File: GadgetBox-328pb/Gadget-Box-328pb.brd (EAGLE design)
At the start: 93.5 x 53.5 mm, 35 parts, among them IC1A ATMEGA328PB-AU, IC1B ATMEGA328PB-MU, U1 MCP73831T-2ACI/OT, U2 AP2112-3.3, X1 CRYSTAL-0500290P1

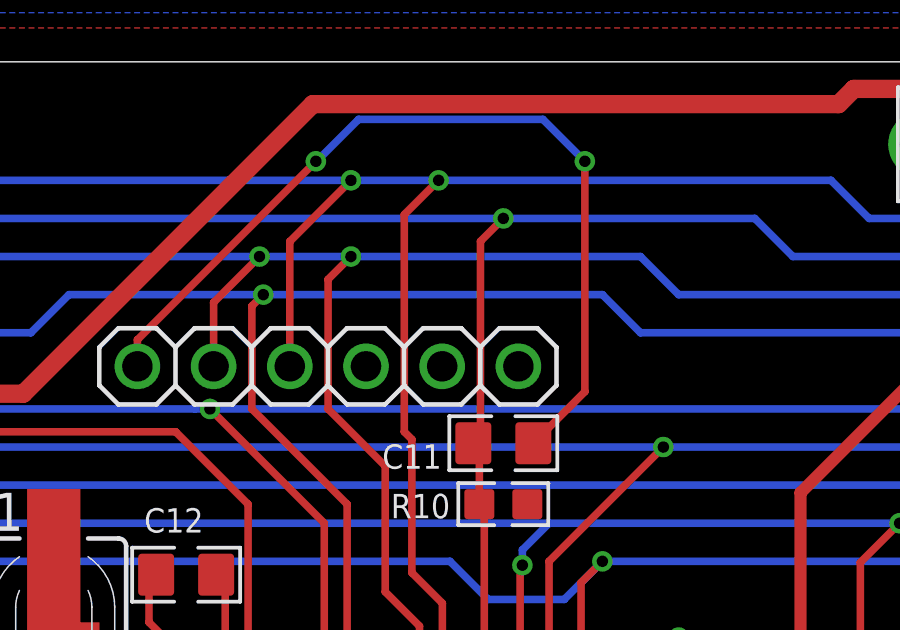
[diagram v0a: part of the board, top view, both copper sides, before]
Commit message: Add resistor to prevent 3.3V from FTDI Module.
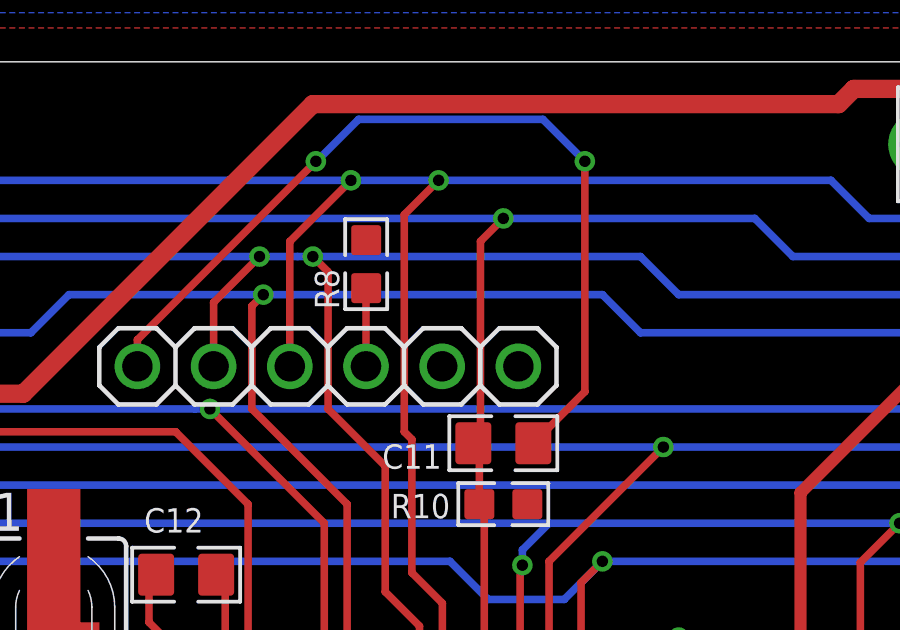
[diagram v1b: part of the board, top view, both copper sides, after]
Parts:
- added R8: 0, GadgetFactory:0603
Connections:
- new net N$7: FTDI.4, R8.1
- net 3V3: now also R8.2; no longer FTDI.4
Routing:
- net N$7: track 0.00 -> 2.61 mm
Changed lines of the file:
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@@
 <layer number="155" name="FabDoc3" color="7" fill="15" visible="no" active="no"/>
 <layer number="199" name="Contour" color="7" fill="1" visible="no" active="yes"/>
-<layer number="200" name="200bmp" color="1" fill="1" visible="yes" active="yes"/>
+<layer number="200" name="200bmp" color="1" fill="1" visible="no" active="yes"/>
 <layer number="201" name="201bmp" color="7" fill="1" visible="no" active="yes"/>
 <layer number="202" name="202bmp" color="7" fill="1" visible="no" active="yes"/>
@@
 <attribute name="PARTNO" value="ABLS-8.000MHZ-B4-T,Abracon Corporation,dk,535-10212-1-ND ,8MHz ±30ppm Crystal 18pF 80 Ohm -20°C ~ 70°C Surface Mount HC49/US , REF102" x="38.862" y="33.147" size="1.778" layer="27" rot="R90" display="off"/>
 </element>
+<element name="R8" library="GadgetFactory" package="0603" value="0" x="49.276" y="48.006" rot="R90">
+<attribute name="BOM" value="EXCLUDE" x="49.276" y="48.006" size="1.778" layer="27" rot="R90" display="off"/>
+</element>
 </elements>
 <signals>
@@
 <wire x1="29.21" y1="46.99" x2="30.48" y2="48.26" width="0.254" layer="16"/>
 <wire x1="30.48" y1="48.26" x2="45.72" y2="48.26" width="0.254" layer="16"/>
-<wire x1="45.72" y1="48.26" x2="48.768" y2="48.26" width="0.254" layer="16"/>
-<wire x1="48.768" y1="48.26" x2="58.42" y2="48.26" width="0.254" layer="16"/>
+<wire x1="45.72" y1="48.26" x2="46.99" y2="48.26" width="0.254" layer="16"/>
+<wire x1="47.498" y1="48.26" x2="58.42" y2="48.26" width="0.254" layer="16"/>
 <wire x1="58.42" y1="48.26" x2="59.69" y2="46.99" width="0.254" layer="16"/>
 <wire x1="59.69" y1="46.99" x2="83.312" y2="46.99" width="0.254" layer="16"/>
@@
 <wire x1="49.6271125" y1="32.3895375" x2="49.6615375" y2="32.3895375" width="0.254" layer="1"/>
 <wire x1="49.6615375" y1="32.3895375" x2="51.054" y2="33.782" width="0.254" layer="1"/>
-<wire x1="48.006" y1="43.18" x2="48.006" y2="47.498" width="0.254" layer="1"/>
-<wire x1="48.006" y1="47.498" x2="48.768" y2="48.26" width="0.254" layer="1"/>
-<via x="48.768" y="48.26" extent="1-16" drill="0.381"/>
 <wire x1="48.88988125" y1="30.59165" x2="48.88988125" y2="30.60188125" width="0.2032" layer="1"/>
 <wire x1="48.88988125" y1="30.60188125" x2="49.276" y2="30.988" width="0.2032" layer="1"/>
@@
 <wire x1="14.478" y1="47.625" x2="13.843" y2="48.26" width="0.254" layer="16"/>
 <wire x1="13.843" y1="48.26" x2="11.43" y2="48.26" width="0.254" layer="16"/>
+<wire x1="48.006" y1="43.18" x2="48.006" y2="47.752" width="0.254" layer="1"/>
+<wire x1="48.006" y1="47.752" x2="47.498" y2="48.26" width="0.254" layer="1"/>
+<via x="47.498" y="48.26" extent="1-16" drill="0.381"/>
+<wire x1="47.498" y1="48.26" x2="46.99" y2="48.26" width="0.254" layer="16"/>
 </signal>
 <signal name="D2*">
@@
 <wire x1="45.7454" y1="30.5562" x2="45.7454" y2="30.766284375" width="0.2032" layer="1"/>
 <wire x1="45.7454" y1="30.766284375" x2="45.253515625" y2="31.25816875" width="0.2032" layer="1"/>
-<contactref element="FTDI" pad="4"/>
 <wire x1="44.577" y1="32.004" x2="44.577" y2="37.35375" width="0.254" layer="1"/>
 <wire x1="44.577" y1="37.35375" x2="44.27525" y2="37.6555" width="0.254" layer="1"/>
+<contactref element="R8" pad="2"/>
 </signal>
 <signal name="5V0">
@@
 <wire x1="46.1772" y1="24.41414375" x2="45.8192" y2="24.05614375" width="0.2032" layer="1"/>
 </signal>
+<signal name="N$7">
+<contactref element="R8" pad="1"/>
+<contactref element="FTDI" pad="4"/>
+<wire x1="49.27" y1="44.6" x2="49.27" y2="47.2" width="0.254" layer="1"/>
+<wire x1="49.27" y1="47.2" x2="49.276" y2="47.206" width="0.254" layer="1"/>
+</signal>
 </signals>

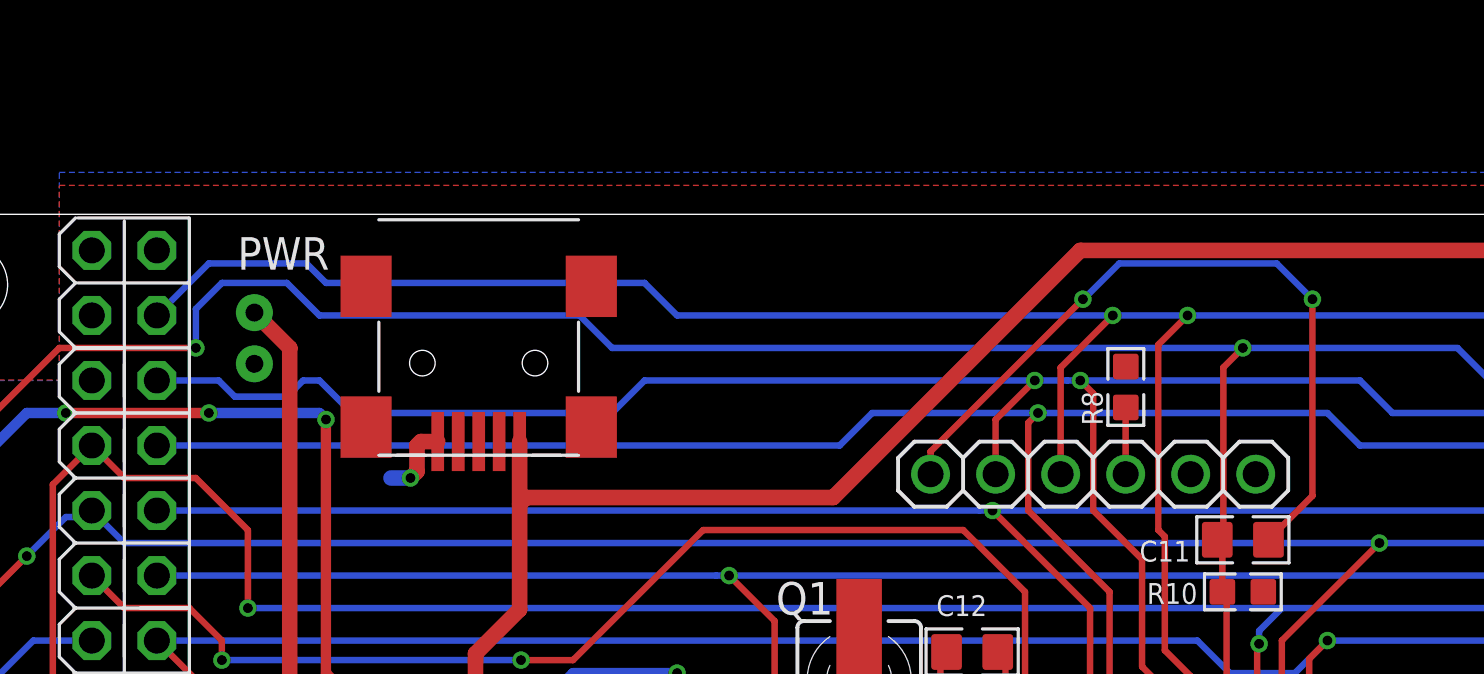
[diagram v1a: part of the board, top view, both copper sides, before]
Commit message: Changed the USB connector per Seeed request.
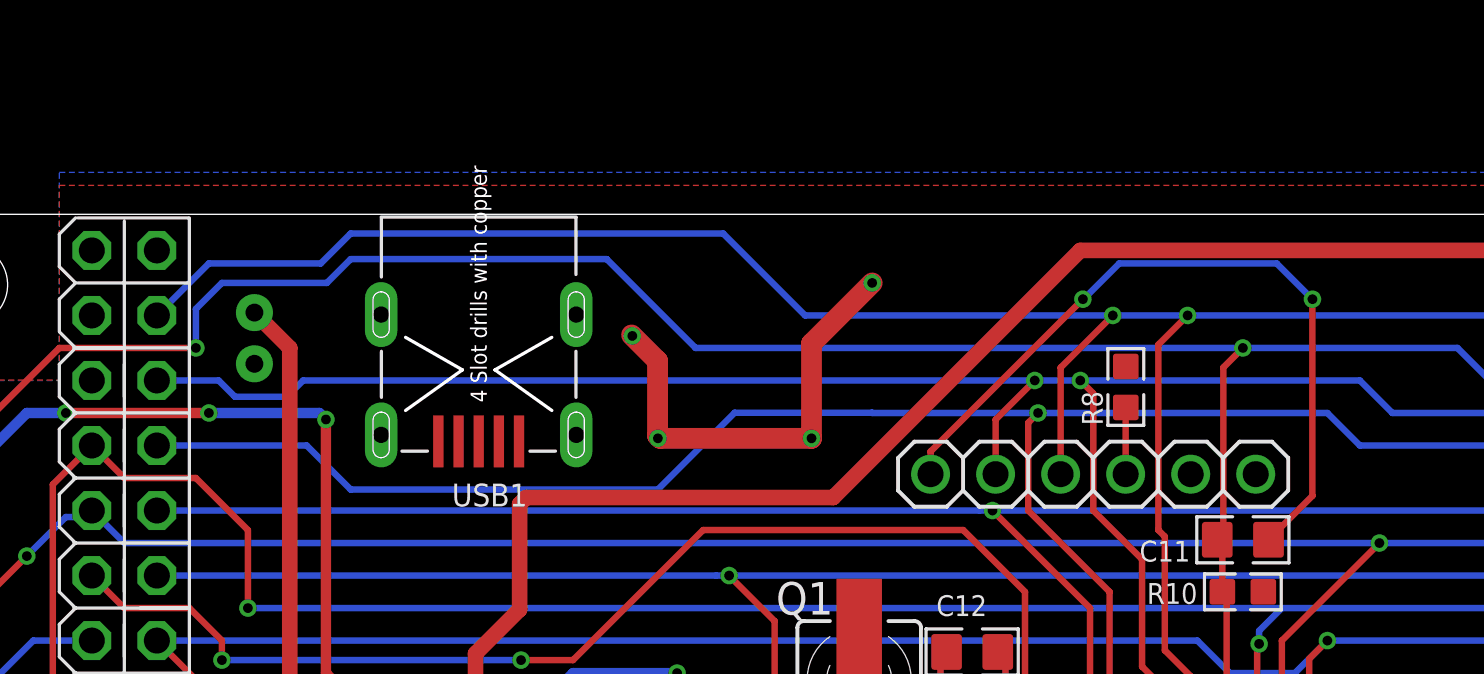
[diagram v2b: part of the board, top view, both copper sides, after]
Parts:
- removed PWR: (no value), adafruit:USB-MINIB
- added USB1: ST-USB-013A, Seeed-OPL-Connector:MINIUSB5+4P-0.8-90D
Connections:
- new net VBUS: USB1.1
- net 5V0: no longer PWR.VBUS
- net GND: now also USB1.GND@1, USB1.GND@2, USB1.GND@3, USB1.GND@4; no longer PWR.GND
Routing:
- net GND: track 55.8 -> 70.3 mm, vias 12 -> 15
- net 5V0: track 224.7 -> 222.3 mm
- net D2*: track 92.3 -> 93.8 mm
- net D1/TX/MOSI: track 100.3 -> 99.3 mm
- net D0/RX/MISO: track 105.6 -> 106.6 mm
- net RESET: track 184.7 -> 185.4 mm
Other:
- board text added: "Gadget Box - ATmega328PB Copyright 2016 Gadget Factory, LLC Version 1.2"
- board text removed: "Gadget Box - ATmega328PB Copyright 2016 Gadget Factory, LLC Version 1.1"

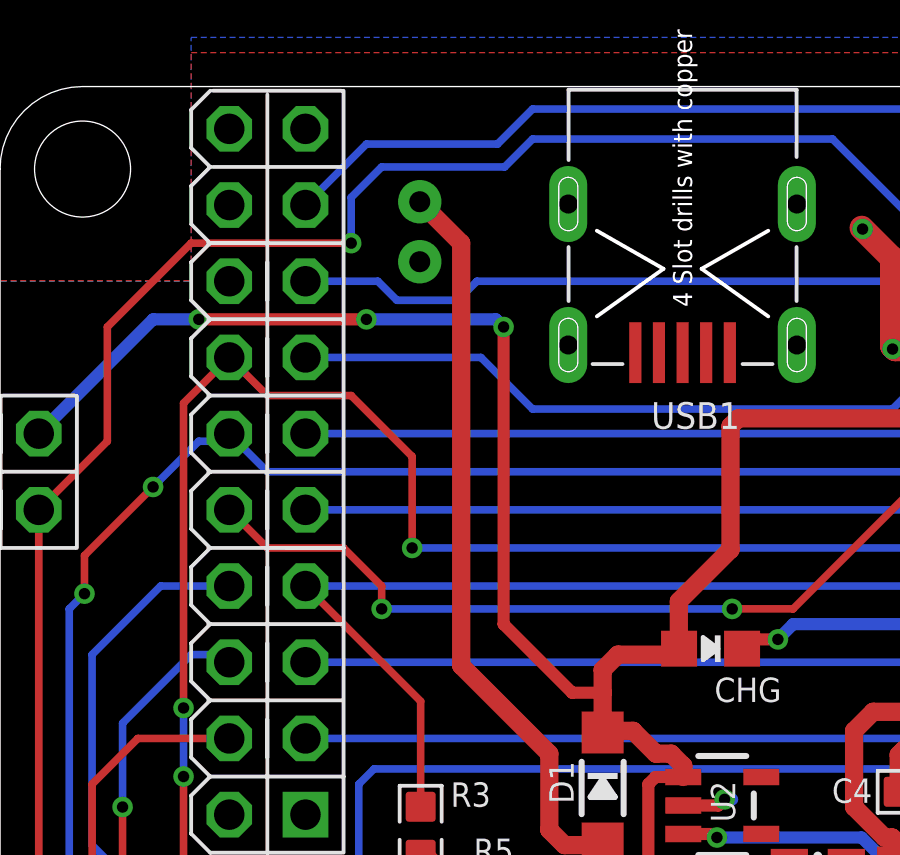
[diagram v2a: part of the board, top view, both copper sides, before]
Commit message: Moved battery connector
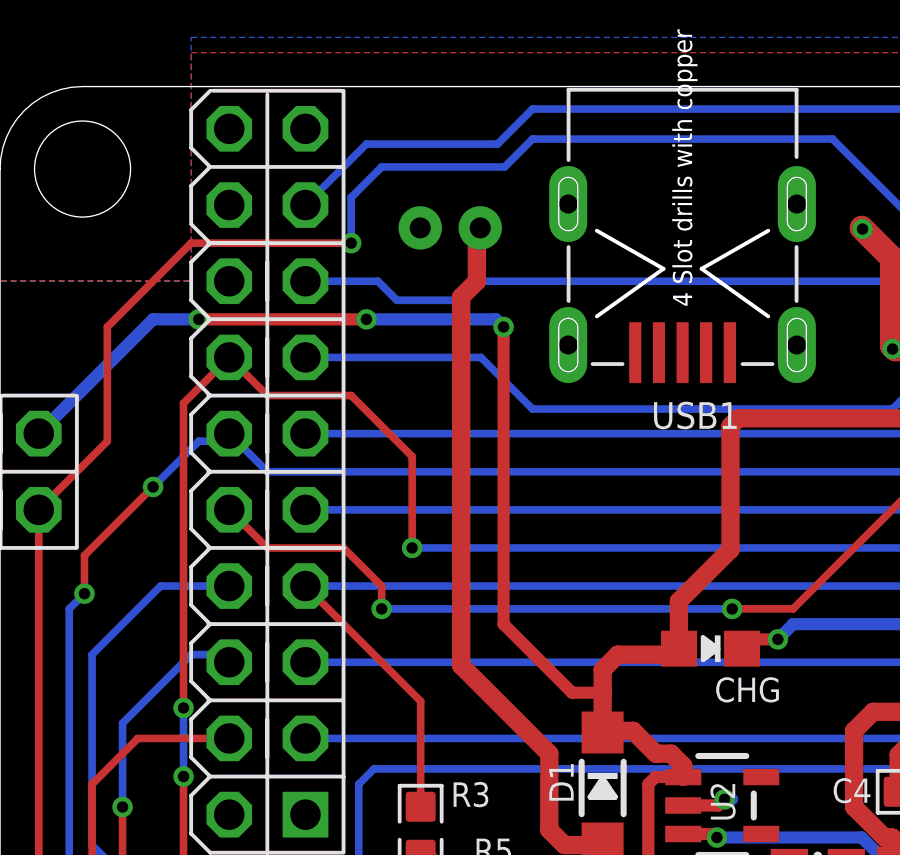
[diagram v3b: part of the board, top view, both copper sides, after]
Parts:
- moved JP1 1.02 mm to (16.3, 50.0), turned to 180 degrees
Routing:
- net VBAT: track 43.2 -> 42.0 mm
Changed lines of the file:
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@@
 <text x="51.78425" y="46.9265" size="0.762" layer="22" font="vector" ratio="15" rot="MR0" align="top-center">Gnd</text>
 <text x="54.32425" y="46.9265" size="0.762" layer="22" font="vector" ratio="15" rot="MR0" align="top-center">Gnd</text>
-<text x="17.78" y="43.18" size="1.778" layer="22" font="vector" ratio="15" rot="MR0">BAT</text>
+<text x="18.542" y="41.783" size="1.778" layer="22" font="vector" ratio="15" rot="MR0">BAT</text>
 <wire x1="67.2296" y1="47.8867" x2="67.2296" y2="47.752" width="0.254" layer="200"/>
 <wire x1="67.2296" y1="47.752" x2="67.2296" y2="47.498" width="0.254" layer="200"/>
@@
 <attribute name="PARTNO" value="RC0603JR-0710KL,YAGEO (VA),dk,311-10KGRCT-ND,RES SMD 10K OHM 5% 1/10W 0603 , REF36" x="66.548" y="28.448" size="1.778" layer="27" display="off"/>
 </element>
-<element name="JP1" library="SparkFun" package="JST-2-PTH-NS" value="" x="15.24" y="49.911" rot="MR90">
-<attribute name="PARTNO" value="B2B-PH-SM4-TB(LF)(SN),JST SALES AMERICA INC (VA),dk,455-1734-1-ND ,&quot;2 Positions Header, Shrouded Connector 0.079 (2.00mm) Through Hole Tin &quot;, REF87" x="15.24" y="49.911" size="1.778" layer="28" rot="MR90" display="off"/>
+<element name="JP1" library="SparkFun" package="JST-2-PTH-NS" value="" x="16.256" y="50.038" rot="MR180">
+<attribute name="PARTNO" value="B2B-PH-SM4-TB(LF)(SN),JST SALES AMERICA INC (VA),dk,455-1734-1-ND ,&quot;2 Positions Header, Shrouded Connector 0.079 (2.00mm) Through Hole Tin &quot;, REF87" x="16.256" y="50.038" size="1.778" layer="28" rot="MR180" display="off"/>
 </element>
 <element name="IC1A" library="we-chip" package="TQFP32" value="ATMEGA328PB-AU" x="48.006" y="27.94" smashed="yes" rot="R315">
@@
 <wire x1="20.066" y1="29.464" x2="21.281" y2="29.464" width="0.6096" layer="1"/>
 <wire x1="21.281" y1="29.464" x2="21.336" y2="29.519" width="0.6096" layer="1"/>
-<wire x1="16.621" y1="35.449" x2="16.621" y2="49.53" width="0.6096" layer="1"/>
-<wire x1="16.621" y1="49.53" x2="15.24" y2="50.911" width="0.6096" layer="1"/>
+<wire x1="16.621" y1="35.449" x2="16.621" y2="47.736" width="0.6096" layer="1"/>
+<wire x1="16.621" y1="47.736" x2="17.145" y2="48.26" width="0.6096" layer="1"/>
+<wire x1="17.145" y1="48.26" x2="17.145" y2="49.927" width="0.6096" layer="1"/>
+<wire x1="17.145" y1="49.927" x2="17.256" y2="50.038" width="0.6096" layer="1"/>
 </signal>
 <signal name="N$1">
